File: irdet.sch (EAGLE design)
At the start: 65 parts, among them IC1 MEGA8-AI, IC2 78L05F, J1 PSH02-04WG, J2 PSH02-04WG, J3 PSH02-04WG, J4 PSH02-04WG, J5 22-05-7098-09, T1 S9013, T2 S9012, T3 S9013, T4 S9012, T5 S9013, T6 S9012, T7 S9013, T8 S9012, X1 ARK500/2

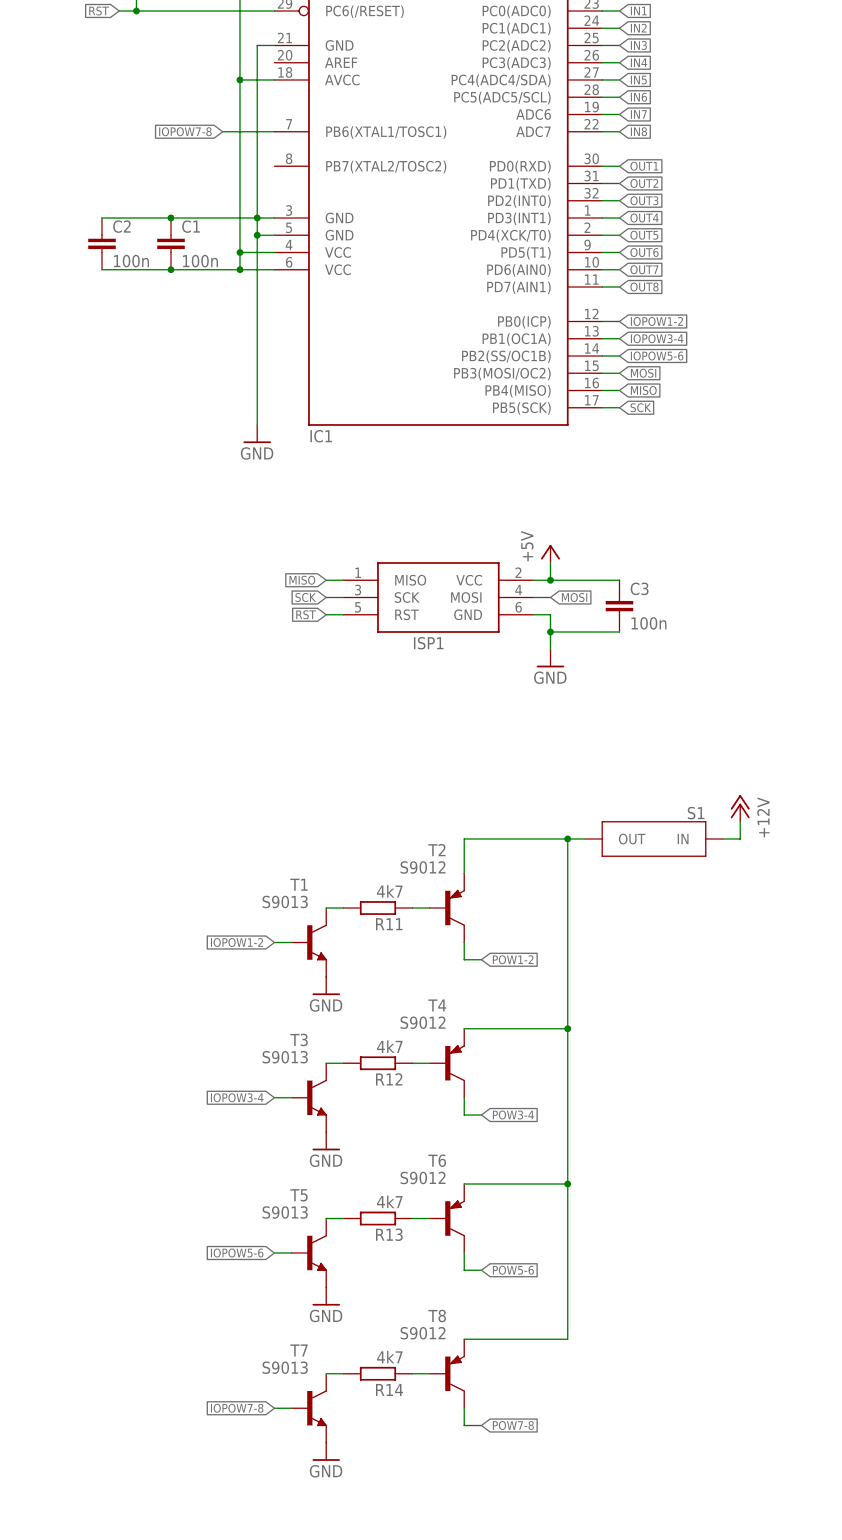
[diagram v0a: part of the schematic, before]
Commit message: IOPOW → CPUPOW.
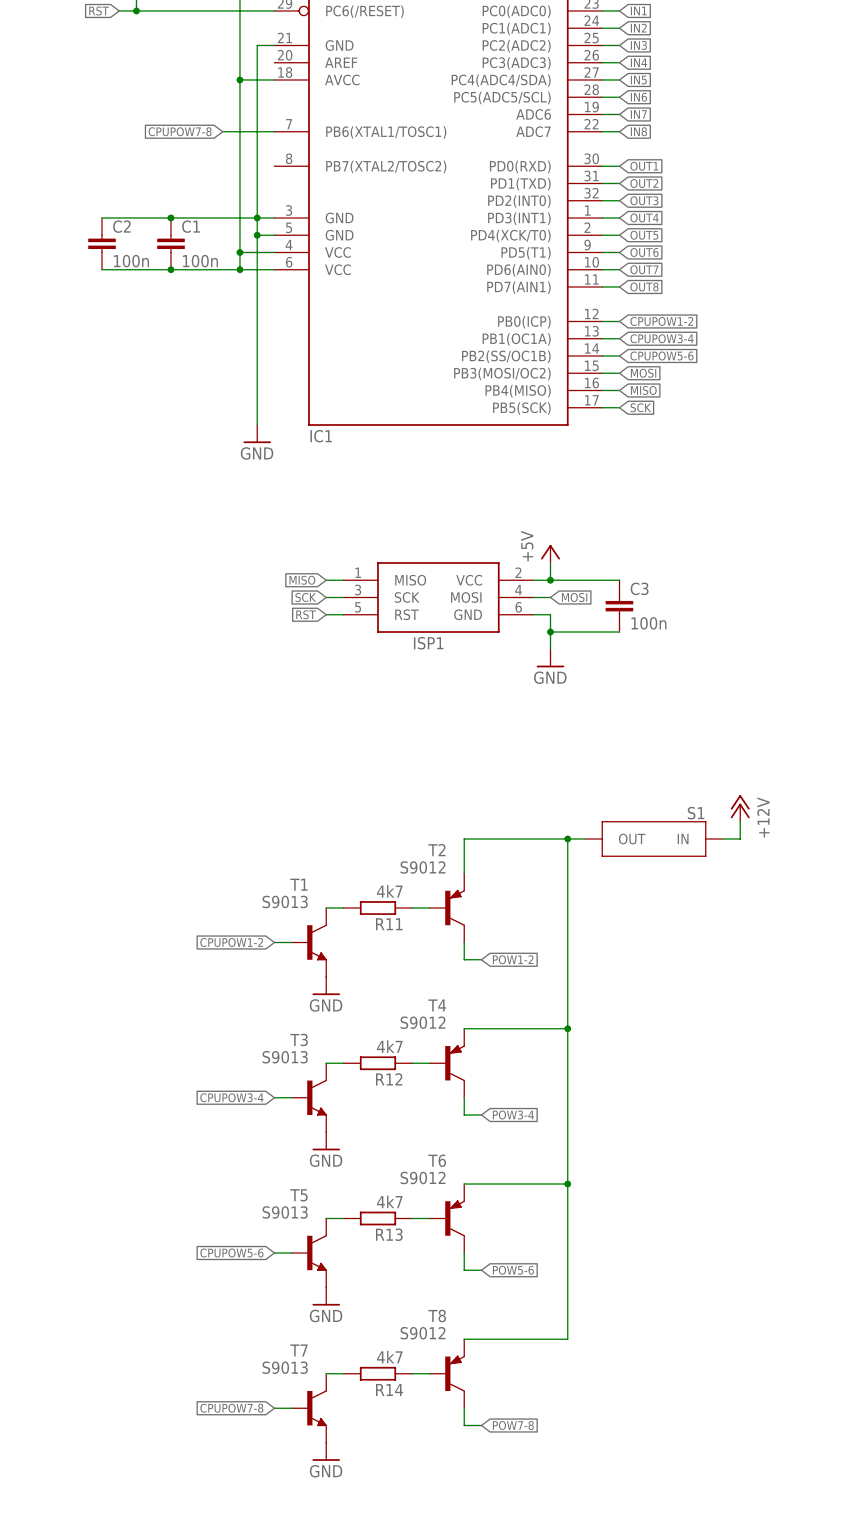
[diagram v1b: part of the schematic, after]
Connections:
- net IOPOW1-2 renamed CPUPOW1-2
- net IOPOW3-4 renamed CPUPOW3-4
- net IOPOW5-6 renamed CPUPOW5-6
- net IOPOW7-8 renamed CPUPOW7-8
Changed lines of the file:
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@@
-</segment>
-</net>
-<net name="IOPOW1-2" class="0">
-<segment>
-<pinref part="T1" gate="G$1" pin="B"/>
-<wire x1="175.26" y1="96.52" x2="172.72" y2="96.52" width="0.1524" layer="91"/>
-<label x="172.72" y="96.52" size="1.27" layer="95" rot="R180" xref="yes"/>
-</segment>
-<segment>
-<pinref part="IC1" gate="G$1" pin="PB0(ICP)"/>
-<wire x1="220.98" y1="187.96" x2="223.52" y2="187.96" width="0.1524" layer="91"/>
-<label x="223.52" y="187.96" size="1.27" layer="95" xref="yes"/>
 </segment>
 </net>
@@
 </segment>
 </net>
-<net name="IOPOW7-8" class="0">
+<net name="CPUPOW7-8" class="0">
 <segment>
 <pinref part="T7" gate="G$1" pin="B"/>
@@
 </segment>
 </net>
-<net name="IOPOW5-6" class="0">
+<net name="CPUPOW5-6" class="0">
 <segment>
 <pinref part="T5" gate="G$1" pin="B"/>
@@
 </segment>
 </net>
-<net name="IOPOW3-4" class="0">
+<net name="CPUPOW3-4" class="0">
 <segment>
 <pinref part="T3" gate="G$1" pin="B"/>
@@
 </segment>
 </net>
+<net name="CPUPOW1-2" class="0">
+<segment>
+<pinref part="T1" gate="G$1" pin="B"/>
+<wire x1="175.26" y1="96.52" x2="172.72" y2="96.52" width="0.1524" layer="91"/>
+<label x="172.72" y="96.52" size="1.27" layer="95" rot="R180" xref="yes"/>
+</segment>
+<segment>
+<pinref part="IC1" gate="G$1" pin="PB0(ICP)"/>
+<wire x1="220.98" y1="187.96" x2="223.52" y2="187.96" width="0.1524" layer="91"/>
+<label x="223.52" y="187.96" size="1.27" layer="95" xref="yes"/>
+</segment>
+</net>

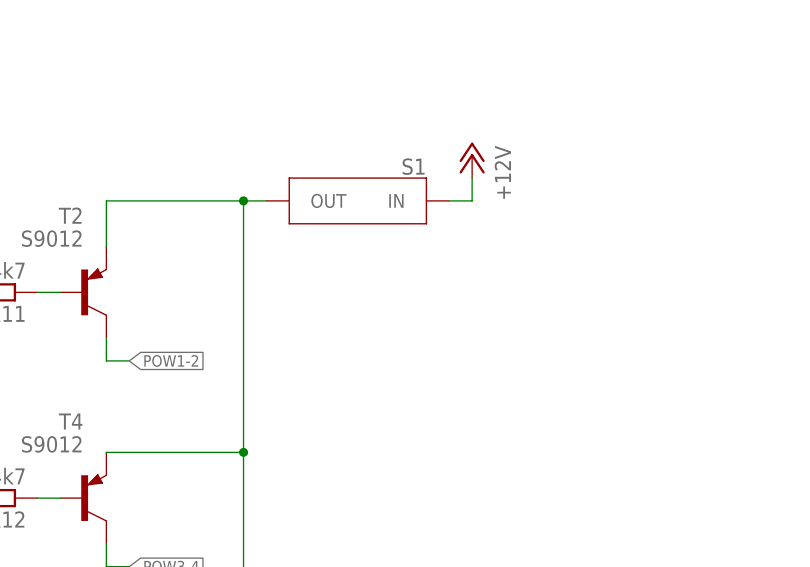
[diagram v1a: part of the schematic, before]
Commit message: Add capacitor to IR power generator.
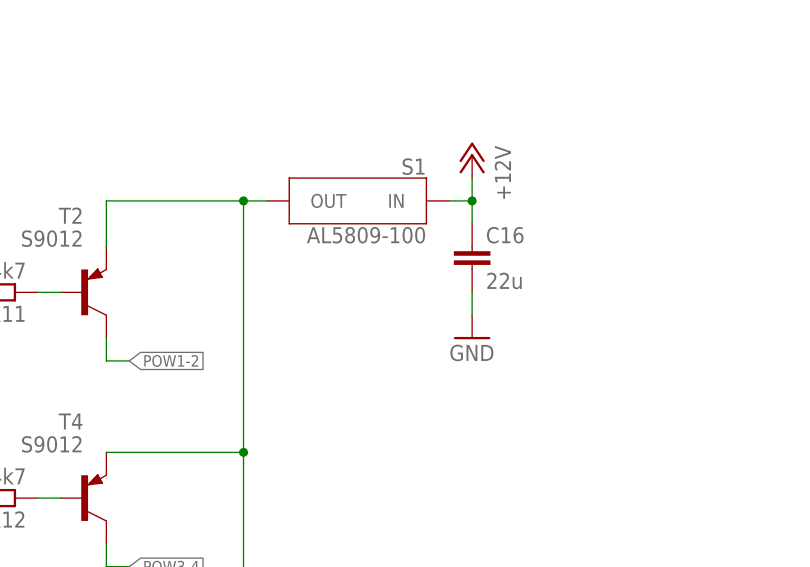
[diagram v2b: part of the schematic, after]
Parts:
- added C16: 22u, rcl:C-EUC0805
- S1: value (none) -> AL5809-100
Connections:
- net +12V: now also C16.1
- net GND: now also C16.2
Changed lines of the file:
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@@
 <part name="GND26" library="supply1" library_urn="urn:adsk.eagle:library:371" deviceset="GND" device=""/>
 <part name="P+9" library="supply1" library_urn="urn:adsk.eagle:library:371" deviceset="+12V" device=""/>
-<part name="S1" library="current-stabilizers" deviceset="AL5809" device=""/>
+<part name="S1" library="current-stabilizers" deviceset="AL5809" device="" value="AL5809-100"/>
 <part name="T3" library="transistor" library_urn="urn:adsk.eagle:library:402" deviceset="*-NPN-" device="SOT23-BEC" package3d_urn="urn:adsk.eagle:package:28748/2" technology="BC808" value="S9013"/>
 <part name="T4" library="transistor" library_urn="urn:adsk.eagle:library:402" deviceset="*-PNP-" device="SOT23-BEC" package3d_urn="urn:adsk.eagle:package:28748/2" technology="BC807-16" value="S9012"/>
@@
 <part name="R14" library="rcl" deviceset="R-EU_" device="R0805" value="4k7"/>
 <part name="GND29" library="supply1" library_urn="urn:adsk.eagle:library:371" deviceset="GND" device=""/>
+<part name="C16" library="rcl" deviceset="C-EU" device="C0805" value="22u"/>
+<part name="GND30" library="supply1" library_urn="urn:adsk.eagle:library:371" deviceset="GND" device=""/>
 </parts>
 <sheets>
@@
 <instance part="GND29" gate="1" x="180.34" y="20.32" smashed="yes">
 <attribute name="VALUE" x="177.8" y="17.78" size="1.778" layer="96"/>
+</instance>
+<instance part="C16" gate="G$1" x="241.3" y="106.68" smashed="yes">
+<attribute name="NAME" x="242.824" y="107.061" size="1.778" layer="95"/>
+<attribute name="VALUE" x="242.824" y="101.981" size="1.778" layer="96"/>
+</instance>
+<instance part="GND30" gate="1" x="241.3" y="96.52" smashed="yes">
+<attribute name="VALUE" x="238.76" y="93.98" size="1.778" layer="96"/>
 </instance>
 </instances>
@@
 <pinref part="GND29" gate="1" pin="GND"/>
 </segment>
+<segment>
+<pinref part="GND30" gate="1" pin="GND"/>
+<pinref part="C16" gate="G$1" pin="2"/>
+<wire x1="241.3" y1="99.06" x2="241.3" y2="101.6" width="0.1524" layer="91"/>
+</segment>
 </net>
 <net name="MISO" class="0">
@@
 <pinref part="P+9" gate="1" pin="+12V"/>
 <wire x1="241.3" y1="111.76" x2="241.3" y2="114.3" width="0.1524" layer="91"/>
-</segment>
-</net>
+<pinref part="C16" gate="G$1" pin="1"/>
+<wire x1="241.3" y1="109.22" x2="241.3" y2="111.76" width="0.1524" layer="91"/>
+<junction x="241.3" y="111.76"/>
+</segment>
+</net>

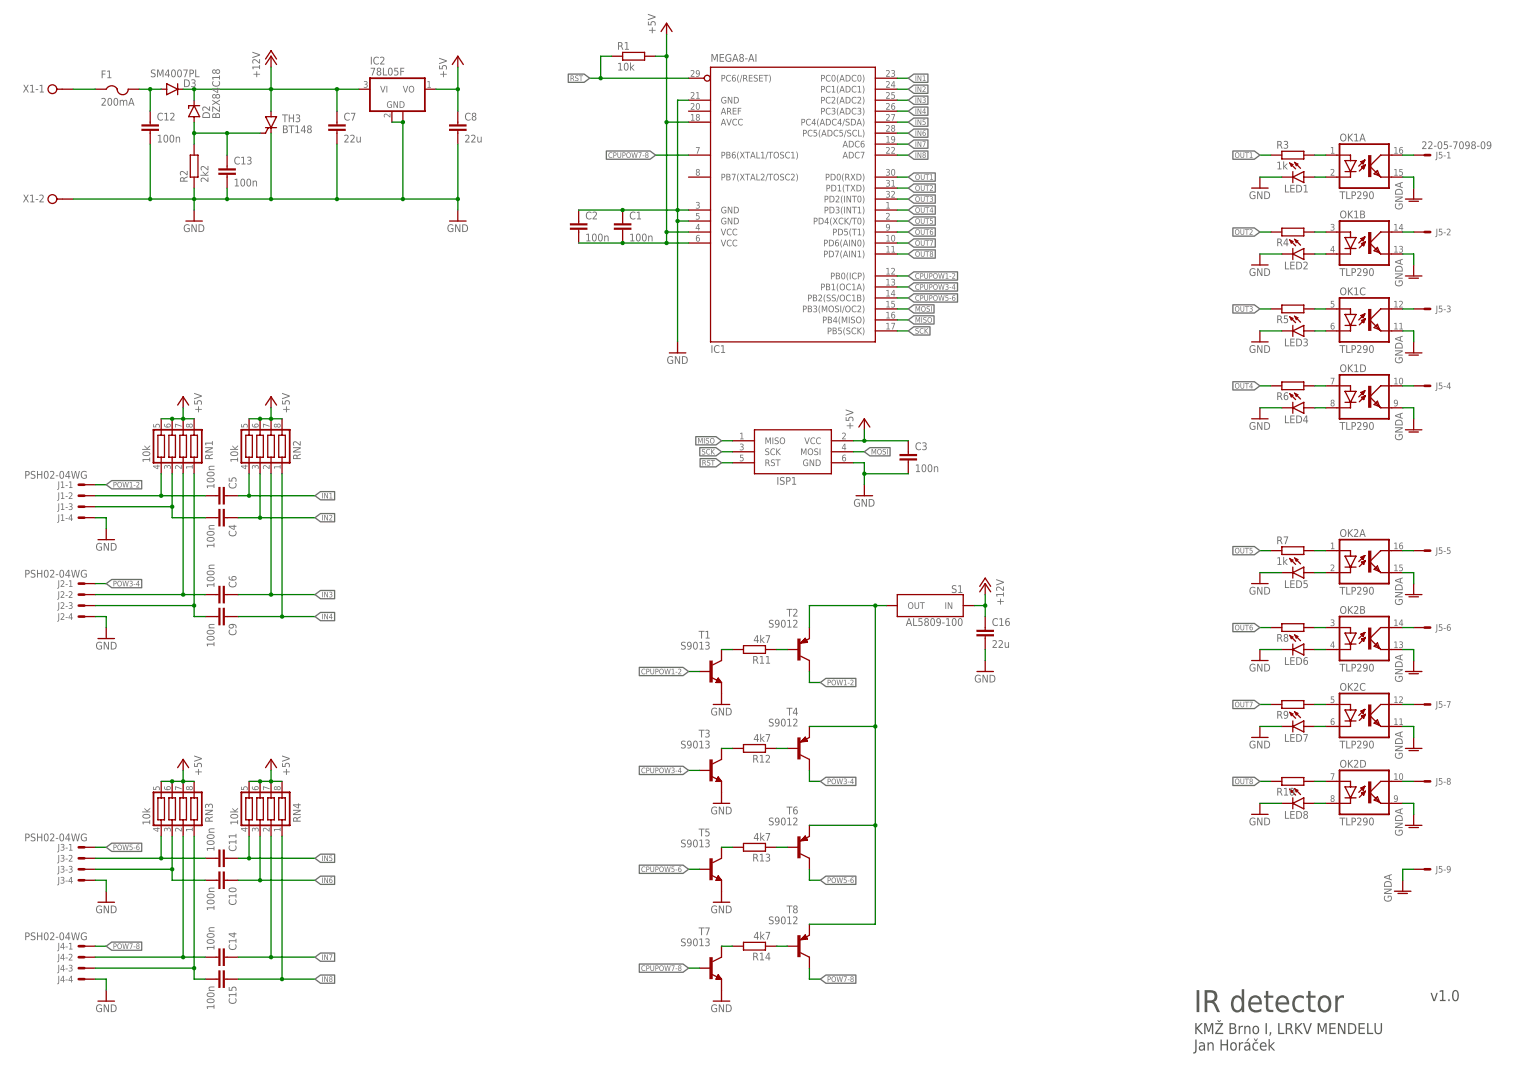
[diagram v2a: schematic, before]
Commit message: Do not use ADC-only inputs of CPU.
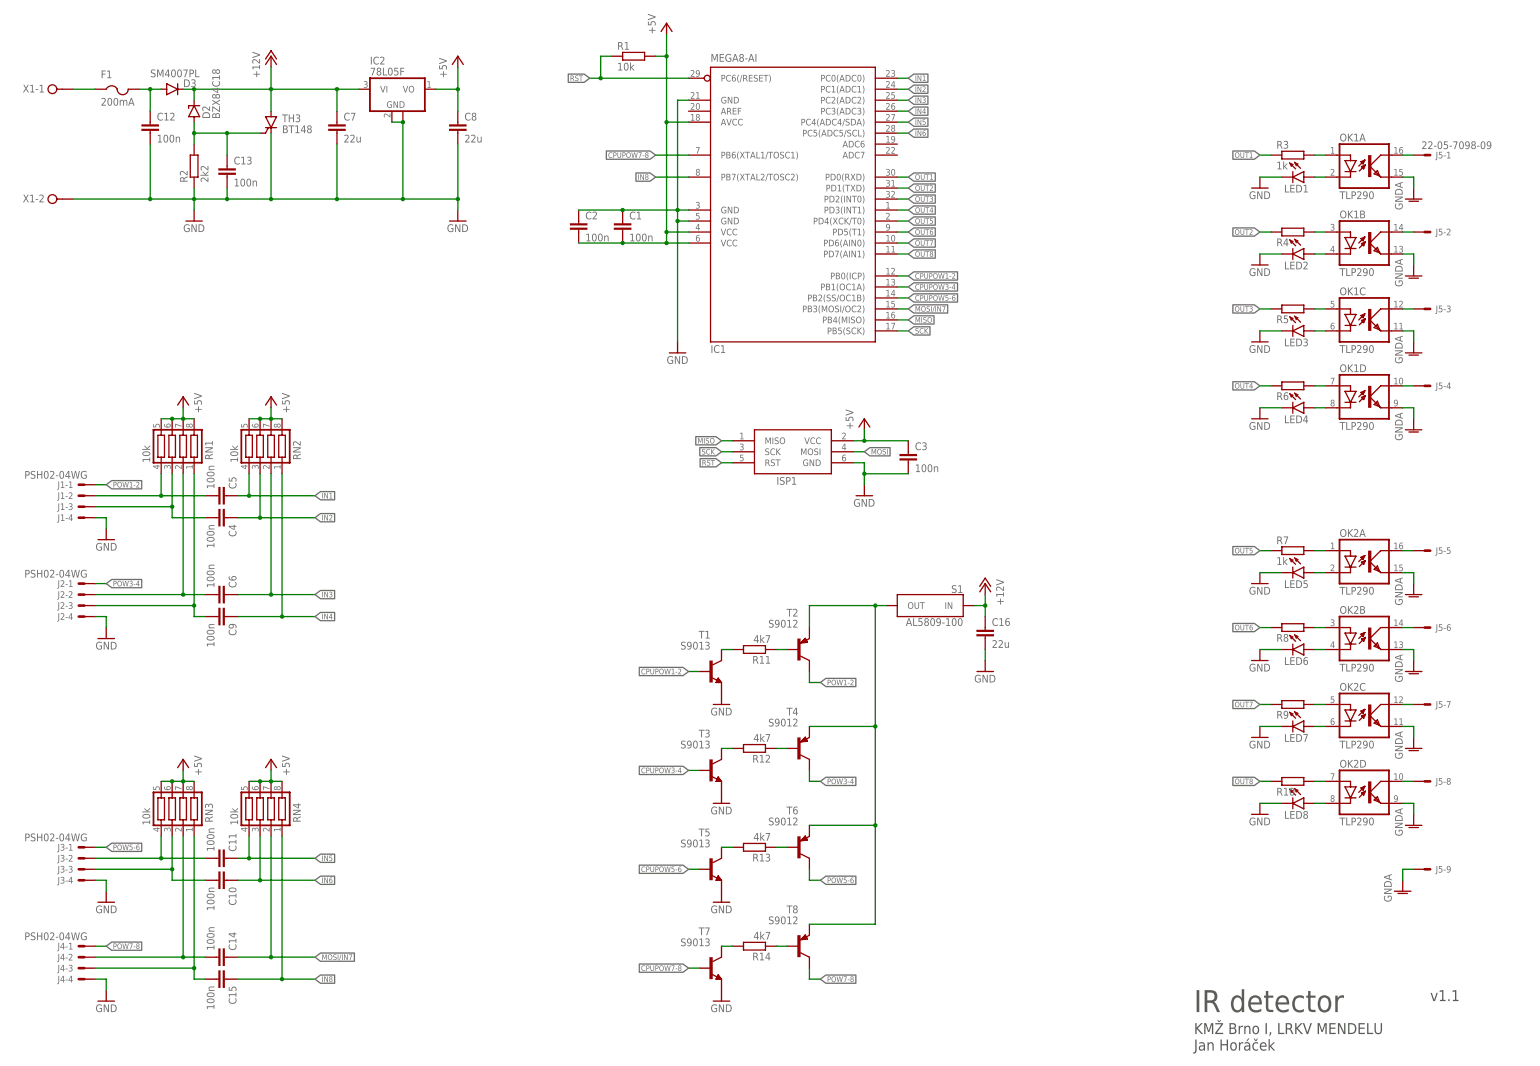
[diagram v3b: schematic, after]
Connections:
- removed net IN7: C14.1, IC1.ADC6, RN4.2
- new net MOSI/IN7: C14.1, IC1.PB3(MOSI/OC2), RN4.2
- net IN8: now also IC1.PB7(XTAL2/TOSC2); no longer IC1.ADC7
- net MOSI: no longer IC1.PB3(MOSI/OC2)
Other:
- note added: "v1.1"
- note removed: "v1.0"
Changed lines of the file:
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@@
 <plain>
 <text x="289.56" y="17.78" size="5.08" layer="97">IR detector</text>
-<text x="344.17" y="20.32" size="2.54" layer="97">v1.0</text>
+<text x="344.17" y="20.32" size="2.54" layer="97">v1.1</text>
 <text x="289.56" y="8.89" size="2.54" layer="97">KMŽ Brno I, LRKV MENDELU
 Jan Horáček</text>
@@
 <net name="MOSI" class="0">
 <segment>
-<pinref part="IC1" gate="G$1" pin="PB3(MOSI/OC2)"/>
-<wire x1="220.98" y1="180.34" x2="223.52" y2="180.34" width="0.1524" layer="91"/>
-<label x="223.52" y="180.34" size="1.27" layer="95" xref="yes"/>
-</segment>
-<segment>
 <pinref part="ISP1" gate="G$1" pin="MOSI"/>
 <wire x1="210.82" y1="147.32" x2="213.36" y2="147.32" width="0.1524" layer="91"/>
@@
 </segment>
 </net>
-<net name="IN7" class="0">
-<segment>
-<pinref part="C14" gate="G$1" pin="1"/>
-<wire x1="68.58" y1="30.48" x2="76.2" y2="30.48" width="0.1524" layer="91"/>
-<pinref part="RN4" gate="G$1" pin="2"/>
-<wire x1="76.2" y1="30.48" x2="76.2" y2="58.42" width="0.1524" layer="91"/>
-<wire x1="76.2" y1="30.48" x2="86.36" y2="30.48" width="0.1524" layer="91"/>
-<junction x="76.2" y="30.48"/>
-<label x="86.36" y="30.48" size="1.27" layer="95" xref="yes"/>
-</segment>
-<segment>
-<pinref part="IC1" gate="G$1" pin="ADC6"/>
-<wire x1="220.98" y1="218.44" x2="223.52" y2="218.44" width="0.1524" layer="91"/>
-<label x="223.52" y="218.44" size="1.27" layer="95" xref="yes"/>
-</segment>
-</net>
 <net name="IN8" class="0">
 <segment>
@@
 </segment>
 <segment>
-<pinref part="IC1" gate="G$1" pin="ADC7"/>
-<wire x1="220.98" y1="215.9" x2="223.52" y2="215.9" width="0.1524" layer="91"/>
-<label x="223.52" y="215.9" size="1.27" layer="95" xref="yes"/>
+<pinref part="IC1" gate="G$1" pin="PB7(XTAL2/TOSC2)"/>
+<wire x1="172.72" y1="210.82" x2="165.1" y2="210.82" width="0.1524" layer="91"/>
+<label x="165.1" y="210.82" size="1.27" layer="95" rot="R180" xref="yes"/>
 </segment>
 </net>
@@
 </segment>
 </net>
+<net name="MOSI/IN7" class="0">
+<segment>
+<pinref part="IC1" gate="G$1" pin="PB3(MOSI/OC2)"/>
+<wire x1="220.98" y1="180.34" x2="223.52" y2="180.34" width="0.1524" layer="91"/>
+<label x="223.52" y="180.34" size="1.27" layer="95" xref="yes"/>
+</segment>
+<segment>
+<pinref part="C14" gate="G$1" pin="1"/>
+<wire x1="68.58" y1="30.48" x2="76.2" y2="30.48" width="0.1524" layer="91"/>
+<pinref part="RN4" gate="G$1" pin="2"/>
+<wire x1="76.2" y1="30.48" x2="76.2" y2="58.42" width="0.1524" layer="91"/>
+<wire x1="76.2" y1="30.48" x2="86.36" y2="30.48" width="0.1524" layer="91"/>
+<junction x="76.2" y="30.48"/>
+<label x="86.36" y="30.48" size="1.27" layer="95" xref="yes"/>
+</segment>
+</net>
